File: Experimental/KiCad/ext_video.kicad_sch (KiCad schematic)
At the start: 30 parts, among them IC13 RT9742SNGV, IC14 TPD4E001DRLR, IC15 TPD4E001DRLR, IC16 TPD12S016PWR, IC17 MIC2026A-1YM-TR, IC18 TPD4E001DRLR, X7 0862-1J1T-43-F, X8 SS-53000-002, X9 5051102091

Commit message: Gerbers update
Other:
- note removed: "Replace with ARJM11B1-502-AB-EW2?"
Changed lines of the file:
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@@
 	(title_block
 		(title "${project_name}")
-		(date "2025-10-16")
+		(date "2025-10-19")
 		(rev "${project_version}")
 		(company "${project_creator}")
@@
 		)
 	)
-	(text "Replace with ARJM11B1-502-AB-EW2?"
-		(exclude_from_sim no)
-		(at 107.95 29.21 0)
-		(effects
-			(font
-				(size 1.27 1.27)
-				(color 255 0 0 1)
-			)
-		)
-	)

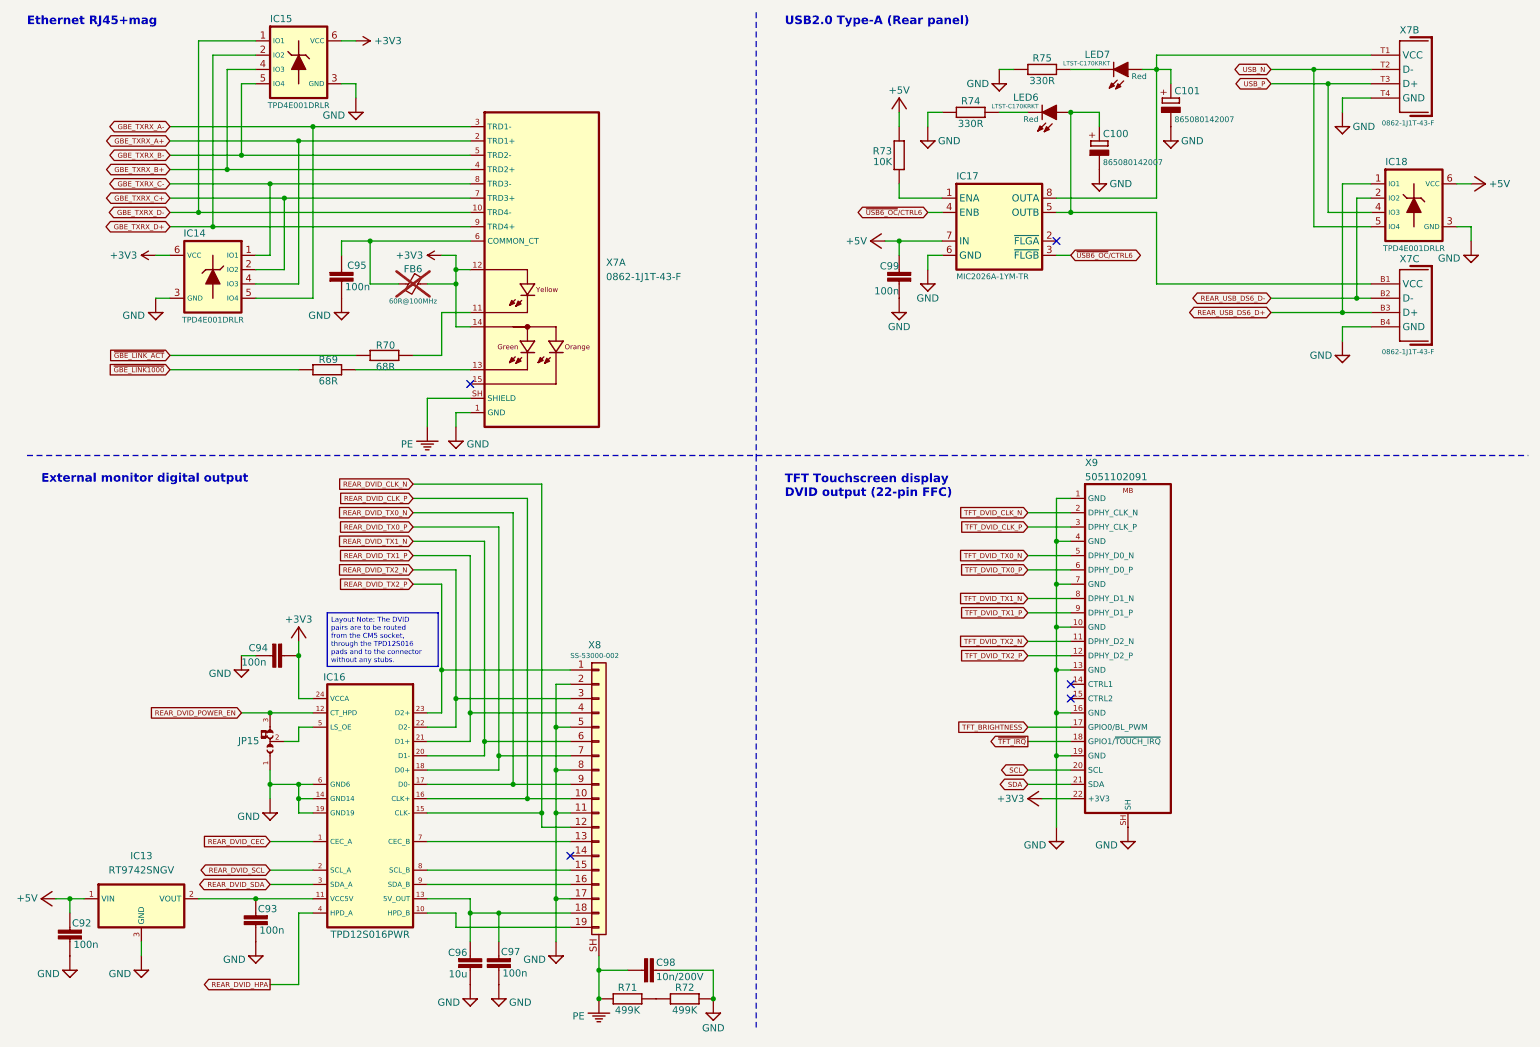
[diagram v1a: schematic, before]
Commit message: Replace 3V3 jumper for H7 CM5 with PMOS sw
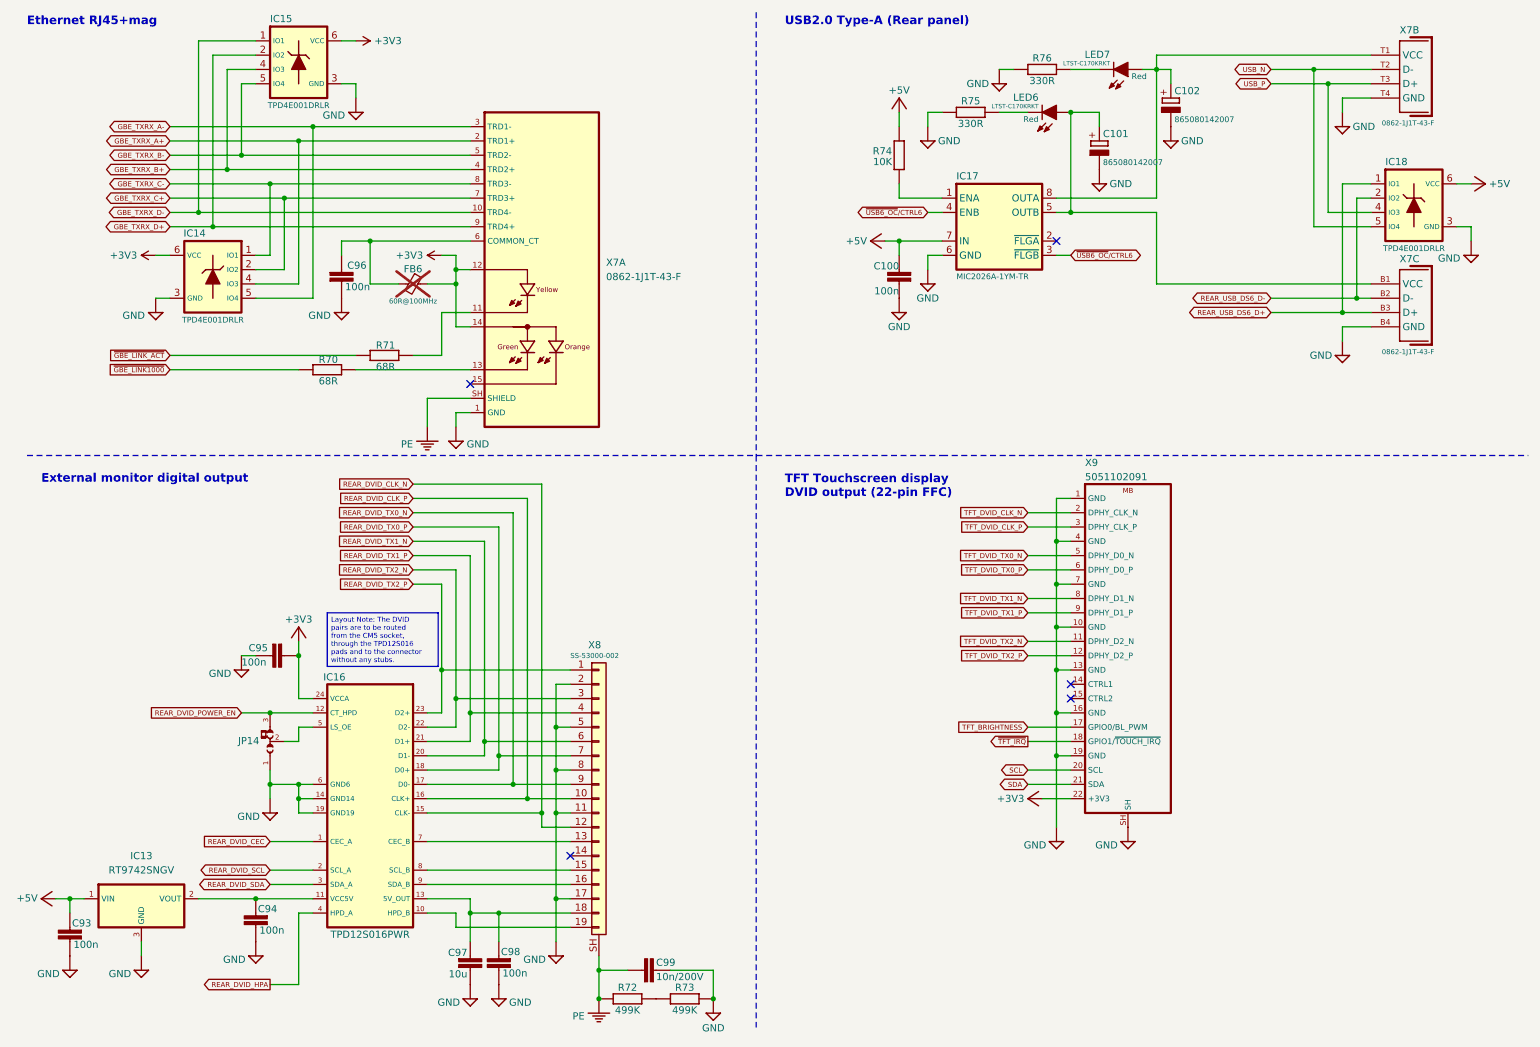
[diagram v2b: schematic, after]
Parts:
- renumbered C99 to C100, C100 to C101, C101 to C102, C92 to C93, C93 to C94, C94 to C95, C95 to C96, C96 to C97, C97 to C98, C98 to C99, JP15 to JP14, R69 to R70, R70 to R71, R71 to R72, R72 to R73, R73 to R74, R74 to R75, R75 to R76
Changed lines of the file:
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@@
 		(on_board yes)
 		(dnp no)
-		(property "Reference" "R75"
+		(property "Reference" "R76"
 			(at 195.58 24.13 90)
 			(effects
@@
 			(project "BB3plus MCU test board"
 				(path "/1df84e4f-233a-4f72-9418-c0020706bb76/c0a485a3-023d-4313-ae06-c16e1fdbf75a"
-					(reference "R75")
+					(reference "R76")
 					(unit 1)
 				)
@@
 		(on_board yes)
 		(dnp no)
-		(property "Reference" "#SUPPLY059"
+		(property "Reference" "#SUPPLY060"
 			(at 71.12 68.58 0)
 			(effects
@@
 			(project "BB3plus MCU test board"
 				(path "/1df84e4f-233a-4f72-9418-c0020706bb76/c0a485a3-023d-4313-ae06-c16e1fdbf75a"
-					(reference "#SUPPLY059")
+					(reference "#SUPPLY060")
 					(unit 1)
 				)
@@
 		(on_board yes)
 		(dnp no)
-		(property "Reference" "#+3V027"
+		(property "Reference" "#+3V028"
 			(at 193.04 154.94 0)
 			(effects
@@
 			(project "BB3plus MCU test board"
 				(path "/1df84e4f-233a-4f72-9418-c0020706bb76/c0a485a3-023d-4313-ae06-c16e1fdbf75a"
-					(reference "#+3V027")
+					(reference "#+3V028")
 					(unit 1)
 				)
@@
 		(on_board yes)
 		(dnp no)
-		(property "Reference" "C94"
+		(property "Reference" "C95"
 			(at 54.61 128.905 90)
 			(effects
@@
 			(project "BB3plus MCU test board"
 				(path "/1df84e4f-233a-4f72-9418-c0020706bb76/c0a485a3-023d-4313-ae06-c16e1fdbf75a"
-					(reference "C94")
+					(reference "C95")
 					(unit 1)
 				)
@@
 		(on_board yes)
 		(dnp no)
-		(property "Reference" "R74"
+		(property "Reference" "R75"
 			(at 182.88 31.75 90)
 			(effects
@@
 			(project "BB3plus MCU test board"
 				(path "/1df84e4f-233a-4f72-9418-c0020706bb76/c0a485a3-023d-4313-ae06-c16e1fdbf75a"
-					(reference "R74")
+					(reference "R75")
 					(unit 1)
 				)
@@
 		(on_board yes)
 		(dnp no)
-		(property "Reference" "C100"
+		(property "Reference" "C101"
 			(at 206.375 36.83 0)
 			(effects
@@
 			(project "BB3plus MCU test board"
 				(path "/1df84e4f-233a-4f72-9418-c0020706bb76/c0a485a3-023d-4313-ae06-c16e1fdbf75a"
-					(reference "C100")
+					(reference "C101")
 					(unit 1)
 				)
@@
 		(on_board yes)
 		(dnp no)
-		(property "Reference" "#SUPPLY058"
+		(property "Reference" "#SUPPLY059"
 			(at 38.1 68.58 0)
 			(effects
@@
 			(project "BB3plus MCU test board"
 				(path "/1df84e4f-233a-4f72-9418-c0020706bb76/c0a485a3-023d-4313-ae06-c16e1fdbf75a"
-					(reference "#SUPPLY058")
+					(reference "#SUPPLY059")
 					(unit 1)
 				)
@@
 		(on_board yes)
 		(dnp no)
-		(property "Reference" "R73"
+		(property "Reference" "R74"
 			(at 168.91 40.64 0)
 			(effects
@@
 			(project "BB3plus MCU test board"
 				(path "/1df84e4f-233a-4f72-9418-c0020706bb76/c0a485a3-023d-4313-ae06-c16e1fdbf75a"
-					(reference "R73")
+					(reference "R74")
 					(unit 1)
 				)
@@
 		(on_board yes)
 		(dnp no)
-		(property "Reference" "C92"
+		(property "Reference" "C93"
 			(at 26.67 177.8 0)
 			(effects
@@
 			(project "BB3plus MCU test board"
 				(path "/1df84e4f-233a-4f72-9418-c0020706bb76/c0a485a3-023d-4313-ae06-c16e1fdbf75a"
-					(reference "C92")
+					(reference "C93")
 					(unit 1)
 				)
@@
 		(on_board yes)
 		(dnp no)
-		(property "Reference" "R72"
+		(property "Reference" "R73"
 			(at 132.08 189.23 90)
 			(effects
@@
 			(project "BB3plus MCU test board"
 				(path "/1df84e4f-233a-4f72-9418-c0020706bb76/c0a485a3-023d-4313-ae06-c16e1fdbf75a"
-					(reference "R72")
+					(reference "R73")
 					(unit 1)
 				)
@@
 		(on_board yes)
 		(dnp no)
-		(property "Reference" "#SUPPLY062"
+		(property "Reference" "#SUPPLY063"
 			(at 271.78 58.42 0)
 			(effects
@@
 			(project "BB3plus MCU test board"
 				(path "/1df84e4f-233a-4f72-9418-c0020706bb76/c0a485a3-023d-4313-ae06-c16e1fdbf75a"
-					(reference "#SUPPLY062")
+					(reference "#SUPPLY063")
 					(unit 1)
 				)
@@
 		(on_board yes)
 		(dnp no)
-		(property "Reference" "R69"
+		(property "Reference" "R70"
 			(at 70.485 76.2 90)
 			(effects
@@
 			(project "BB3plus MCU test board"
 				(path "/1df84e4f-233a-4f72-9418-c0020706bb76/c0a485a3-023d-4313-ae06-c16e1fdbf75a"
-					(reference "R69")
+					(reference "R70")
 					(unit 1)
 				)
@@
 		(on_board yes)
 		(dnp no)
-		(property "Reference" "C96"
+		(property "Reference" "C97"
 			(at 93.472 183.0324 0)
 			(effects
@@
 			(project "BB3plus MCU test board"
 				(path "/1df84e4f-233a-4f72-9418-c0020706bb76/c0a485a3-023d-4313-ae06-c16e1fdbf75a"
-					(reference "C96")
+					(reference "C97")
 					(unit 1)
 				)
@@
 		(on_board yes)
 		(dnp no)
-		(property "Reference" "#SUPPLY061"
+		(property "Reference" "#SUPPLY062"
 			(at 91.44 91.44 0)
 			(effects
@@
 			(project "BB3plus MCU test board"
 				(path "/1df84e4f-233a-4f72-9418-c0020706bb76/c0a485a3-023d-4313-ae06-c16e1fdbf75a"
-					(reference "#SUPPLY061")
+					(reference "#SUPPLY062")
 					(unit 1)
 				)
@@
 		(on_board yes)
 		(dnp no)
-		(property "Reference" "C97"
+		(property "Reference" "C98"
 			(at 102.87 182.88 0)
 			(effects
@@
 			(project "BB3plus MCU test board"
 				(path "/1df84e4f-233a-4f72-9418-c0020706bb76/c0a485a3-023d-4313-ae06-c16e1fdbf75a"
-					(reference "C97")
+					(reference "C98")
 					(unit 1)
 				)
@@
 		(on_board yes)
 		(dnp no)
-		(property "Reference" "#+3V026"
+		(property "Reference" "#+3V027"
 			(at 63.5 124.46 0)
 			(effects
@@
 			(project "BB3plus MCU test board"
 				(path "/1df84e4f-233a-4f72-9418-c0020706bb76/c0a485a3-023d-4313-ae06-c16e1fdbf75a"
-					(reference "#+3V026")
+					(reference "#+3V027")
 					(unit 1)
 				)
@@
 		(on_board yes)
 		(dnp no)
-		(property "Reference" "C93"
+		(property "Reference" "C94"
 			(at 59.69 175.26 0)
 			(effects
@@
 			(project "BB3plus MCU test board"
 				(path "/1df84e4f-233a-4f72-9418-c0020706bb76/c0a485a3-023d-4313-ae06-c16e1fdbf75a"
-					(reference "C93")
+					(reference "C94")
 					(unit 1)
 				)
@@
 		(on_board yes)
 		(dnp no)
-		(property "Reference" "C95"
+		(property "Reference" "C96"
 			(at 75.565 60.96 0)
 			(effects
@@
 			(project "BB3plus MCU test board"
 				(path "/1df84e4f-233a-4f72-9418-c0020706bb76/c0a485a3-023d-4313-ae06-c16e1fdbf75a"
-					(reference "C95")
+					(reference "C96")
 					(unit 1)
 				)
@@
 		(on_board yes)
 		(dnp no)
-		(property "Reference" "R71"
+		(property "Reference" "R72"
 			(at 121.92 189.23 90)
 			(effects
@@
 			(project "BB3plus MCU test board"
 				(path "/1df84e4f-233a-4f72-9418-c0020706bb76/c0a485a3-023d-4313-ae06-c16e1fdbf75a"
-					(reference "R71")
+					(reference "R72")
 					(unit 1)
 				)
@@
 		(on_board yes)
 		(dnp no)
-		(property "Reference" "JP15"
+		(property "Reference" "JP14"
 			(at 56.515 145.415 90)
 			(effects
@@
 			(project "BB3plus MCU test board"
 				(path "/1df84e4f-233a-4f72-9418-c0020706bb76/c0a485a3-023d-4313-ae06-c16e1fdbf75a"
-					(reference "JP15")
+					(reference "JP14")
 					(unit 1)
 				)
@@
 		(on_board yes)
 		(dnp no)
-		(property "Reference" "R70"
+		(property "Reference" "R71"
 			(at 80.645 73.66 90)
 			(effects
@@
 			(project "BB3plus MCU test board"
 				(path "/1df84e4f-233a-4f72-9418-c0020706bb76/c0a485a3-023d-4313-ae06-c16e1fdbf75a"
-					(reference "R70")
+					(reference "R71")
 					(unit 1)
 				)
@@
 		(on_board yes)
 		(dnp no)
-		(property "Reference" "C99"
+		(property "Reference" "C100"
 			(at 170.18 60.325 0)
 			(effects
@@
 			(project "BB3plus MCU test board"
 				(path "/1df84e4f-233a-4f72-9418-c0020706bb76/c0a485a3-023d-4313-ae06-c16e1fdbf75a"
-					(reference "C99")
+					(reference "C100")
 					(unit 1)
 				)
@@
 		(on_board yes)
 		(dnp no)
-		(property "Reference" "C98"
+		(property "Reference" "C99"
 			(at 127 184.785 90)
 			(effects
@@
 			(project "BB3plus MCU test board"
 				(path "/1df84e4f-233a-4f72-9418-c0020706bb76/c0a485a3-023d-4313-ae06-c16e1fdbf75a"
-					(reference "C98")
+					(reference "C99")
 					(unit 1)
 				)
@@
 		(on_board yes)
 		(dnp no)
-		(property "Reference" "C101"
+		(property "Reference" "C102"
 			(at 219.075 29.21 0)
 			(effects
@@
 			(project "BB3plus MCU test board"
 				(path "/1df84e4f-233a-4f72-9418-c0020706bb76/c0a485a3-023d-4313-ae06-c16e1fdbf75a"
-					(reference "C101")
+					(reference "C102")
 					(unit 1)
 				)
@@
 		(on_board yes)
 		(dnp no)
-		(property "Reference" "#SUPPLY060"
+		(property "Reference" "#SUPPLY061"
 			(at 73.66 33.02 0)
 			(effects
@@
 			(project "BB3plus MCU test board"
 				(path "/1df84e4f-233a-4f72-9418-c0020706bb76/c0a485a3-023d-4313-ae06-c16e1fdbf75a"
-					(reference "#SUPPLY060")
+					(reference "#SUPPLY061")
 					(unit 1)
 				)

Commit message: Jumpers update
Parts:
- added JP15, JP16: ~, PCM_EEZ_SMD:JP3 shorted with 0R (0603) 2-3, symbol PCM_EEZ_unsorted:JP3 shorted with 0R (2-3)
- JP14: value ~ -> 0R; now in the parts list
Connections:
- net SCL: now also JP15.3; no longer X9.20 (SCL)
- net SDA: now also JP16.3; no longer X9.21 (SDA)
- net TFT_DVID_HPA: now reaches X9.14 (CTRL1)
- net TFT_DVID_CEC: now reaches X9.15 (CTRL2)
- new net: JP15.2, X9.20 (SCL)
- new net: JP16.2, X9.21 (SDA)
- new net TFT_DVID_SCL: JP15.1
- new net TFT_DVID_SDA: JP16.1
- no-connect marks 5 -> 3
